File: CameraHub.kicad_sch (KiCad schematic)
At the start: 20 parts, among them J1 200528-0120, J10 Header 01x04 0.1", J11 Header 01x04 0.1", J2 Conn_01x02, J3 Conn_01x02, U14 TLV76733QWDRBxQ1

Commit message: Complete layout
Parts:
- removed J2, J3: Conn_01x02, Connector_JST:JST_PH_S2B-PH-SM4-TB_1x02-1MP_P2.00mm_Horizontal, symbol Connector_Generic_MountingPin:Conn_01x02_MountingPin
- added J10: TE_282834-4, CameraHub:TE_282834-4, symbol Connector_Generic:Conn_01x04
- J1: value 200528-0120 -> 200528-0100; footprint Connector_FFC-FPC:Molex_200528-0120_1x12-1MP_P1.00mm_Horizontal -> Connector_FFC-FPC:Molex_200528-0100_1x10-1MP_P1.00mm_Horizontal; symbol Connector_Generic_MountingPin:Conn_01x12_MountingPin -> Connector_Generic_MountingPin:Conn_01x10_MountingPin
- renumbered J10 to J2, J11 to J3
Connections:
- net +3.3V: now also J10.1 (Pin_1)
- net +5V: now also J10.3 (Pin_3)
- net GND: now also J1.10 (Pin_10), J1.4 (Pin_4), J10.2 (Pin_2), J10.4 (Pin_4); no longer J1.11 (Pin_11), J1.12 (Pin_12), J1.2 (Pin_2), J1.8 (Pin_8)
- net USB1_N: now also J1.2 (Pin_2); no longer J1.3 (Pin_3)
- net USB1_P: now also J1.3 (Pin_3); no longer J1.4 (Pin_4)
- net USB2_N: now also J1.8 (Pin_8); no longer J1.9 (Pin_9)
- net USB2_P: now also J1.9 (Pin_9); no longer J1.10 (Pin_10)

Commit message: Budged Jetson FPC connector
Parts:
- H1, H2, H3, H4: footprint CameraHub:MountingHole -> CameraHub:MountingHole2
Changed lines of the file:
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@@
 			)
 		)
-		(property "Footprint" "CameraHub:MountingHole"
+		(property "Footprint" "CameraHub:MountingHole2"
 			(at 50.8 152.4 0)
 			(effects
@@
 			)
 		)
-		(property "Footprint" "CameraHub:MountingHole"
+		(property "Footprint" "CameraHub:MountingHole2"
 			(at 50.8 182.88 0)
 			(effects
@@
 			)
 		)
-		(property "Footprint" "CameraHub:MountingHole"
+		(property "Footprint" "CameraHub:MountingHole2"
 			(at 50.8 172.72 0)
 			(effects
@@
 			)
 		)
-		(property "Footprint" "CameraHub:MountingHole"
+		(property "Footprint" "CameraHub:MountingHole2"
 			(at 50.8 162.56 0)
 			(effects

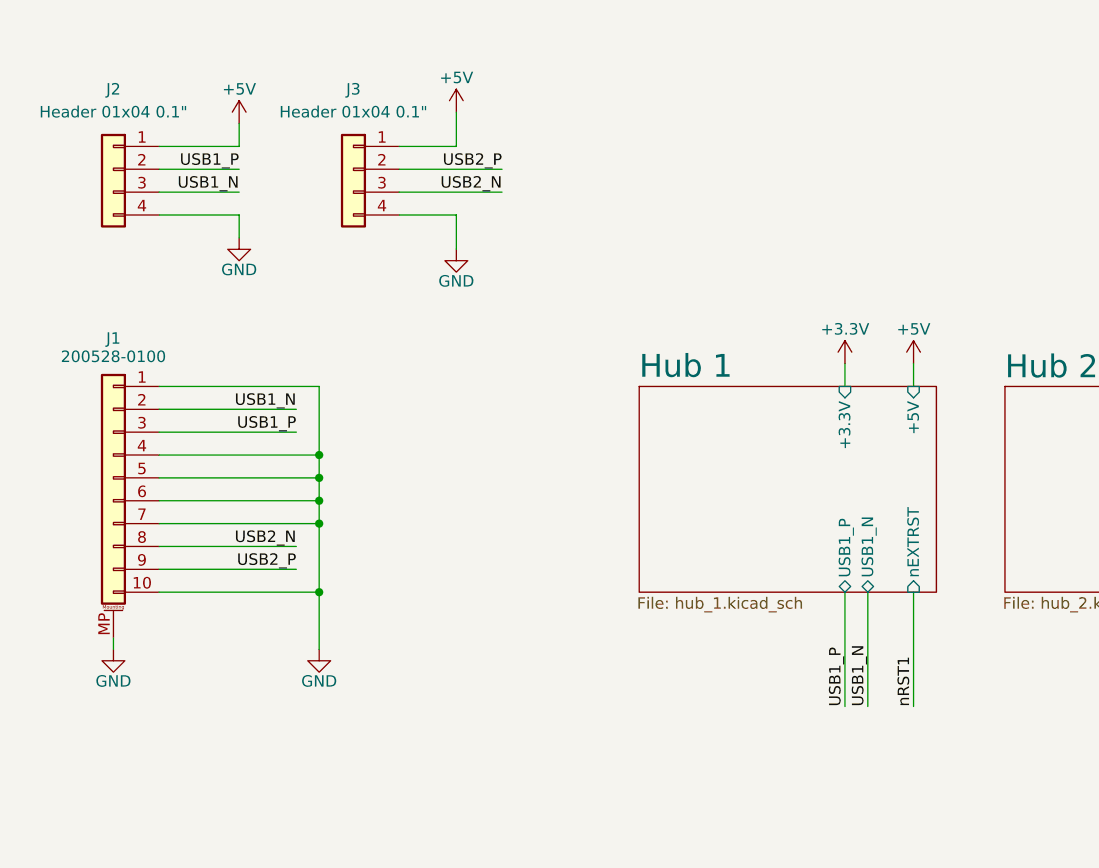
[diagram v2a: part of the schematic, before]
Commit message: Finished Camera Hub
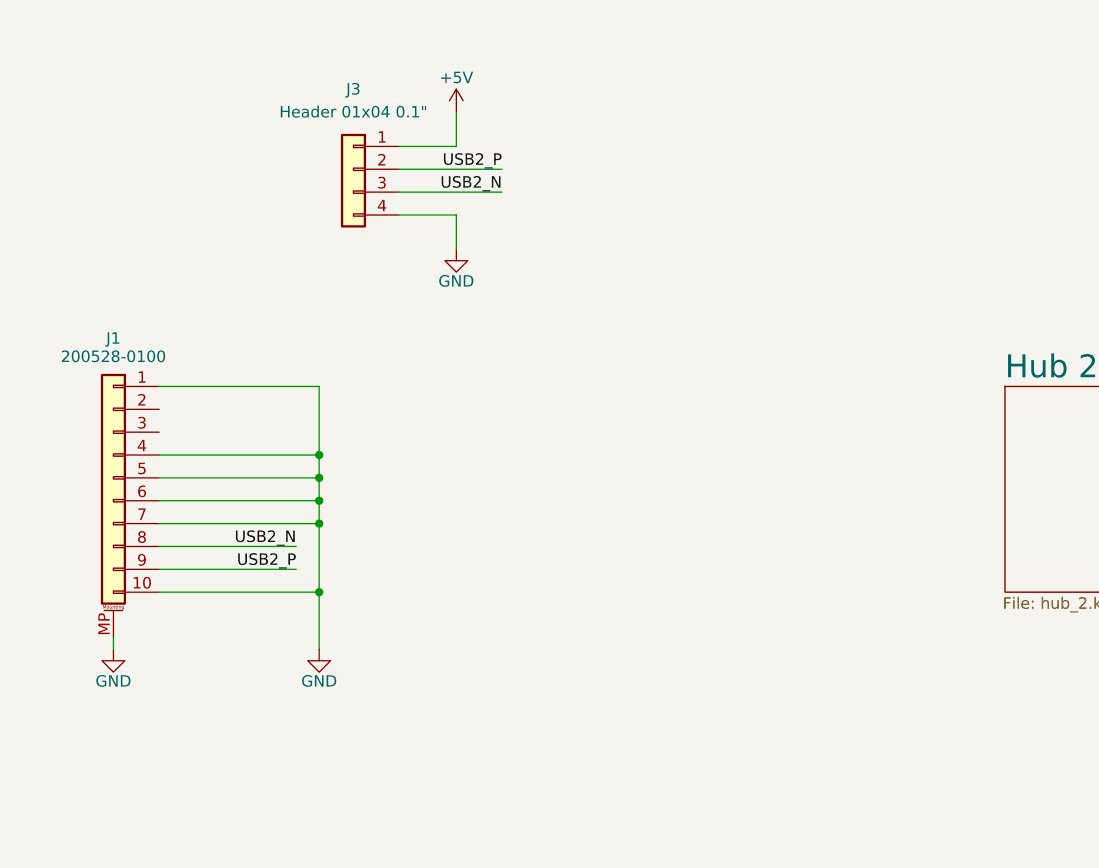
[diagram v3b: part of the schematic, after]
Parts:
- removed J2: Header 01x04 0.1", Connector_PinHeader_2.54mm:PinHeader_1x04_P2.54mm_Vertical, symbol Connector_Generic:Conn_01x04
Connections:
- net USB1_N: no longer names the net of J1.2 (Pin_2)
- net USB1_P: no longer names the net of J1.3 (Pin_3)
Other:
- removed sheet Hub 1

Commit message: rev2.1
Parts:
- removed J1: 200528-0100, Connector_FFC-FPC:Molex_200528-0100_1x10-1MP_P1.00mm_Horizontal, symbol Connector_Generic_MountingPin:Conn_01x10_MountingPin
- removed J10: TE_282834-4, CameraHub:TE_282834-4, symbol Connector_Generic:Conn_01x04
- added C22: 1uF, Capacitor_SMD:C_0603_1608Metric, symbol Device:C_Small
- added J1: Conn_01x01, symbol Connector_Generic:Conn_01x01
- added J5: 200528-0100, Connector_FFC-FPC:Molex_200528-0100_1x10-1MP_P1.00mm_Horizontal, symbol Connector_Generic_MountingPin:Conn_01x10_MountingPin
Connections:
- net +5V: now also C22.2, J5.10 (Pin_10), J5.7 (Pin_7), J5.8 (Pin_8), J5.9 (Pin_9)
- net GND: now also C22.1, J5.1 (Pin_1), J5.4 (Pin_4), J5.5 (Pin_5), J5.6 (Pin_6), J5.MP (MountPin)
- net USB2_N renamed USB_N
- net USB_N: now also J5.2 (Pin_2)
- net USB2_P renamed USB_P
- net USB_P: now also J5.3 (Pin_3)
- new net nRST: J1.1 (Pin_1)
